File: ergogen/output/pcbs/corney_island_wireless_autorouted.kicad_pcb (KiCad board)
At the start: 2 copper layers, 133.8 x 91.7 mm, 68 parts

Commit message: Update assets
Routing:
- net C4: track 201.2 -> 172.0 mm, vias 2 -> 3
- net R0: track 177.9 -> 203.0 mm, vias 11 -> 9
- net R1: track 164.5 -> 185.3 mm, vias 9 -> 8
- net C3: track 208.1 -> 192.2 mm, vias 2 -> 3
- net C5: track 176.6 -> 161.1 mm, vias 4 -> 3
- net C2: track 184.3 -> 172.7 mm, vias 1 -> 2
- net R2: track 176.0 -> 170.6 mm, vias 7 -> 6
- net SDA: track 53.9 -> 50.1 mm, vias 1 -> 2
- net R3: track 133.9 -> 130.5 mm
- net GND: track 105.8 -> 109.1 mm
- net BAT_P: track 60.6 -> 63.7 mm
- net DISP1_5: track 7.38 -> 4.90 mm
- net DISP1_2: track 7.38 -> 4.90 mm
- net DISP1_4: track 7.38 -> 4.90 mm
- net DISP1_1: track 7.38 -> 4.90 mm
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
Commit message: Update assets
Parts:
- removed SW1: , power_switch
- removed SW2: , sw_reset_side
- added MH1: , ceoloide:mounting_hole_npth, F.Cu at (207.8, 100.5)
- added MH2: , ceoloide:mounting_hole_npth, F.Cu at (222.2, 109.0)
- added MH3: , ceoloide:mounting_hole_npth, F.Cu at (109.5, 71.5)
- added MH4: , ceoloide:mounting_hole_npth, F.Cu at (109.5, 90.5)
- added MH5: , ceoloide:mounting_hole_npth, F.Cu at (185.5, 68.0)
- added MH6: , ceoloide:mounting_hole_npth, F.Cu at (152.7, 107.7)
- added MH7: , ceoloide:mounting_hole_npth, F.Cu at (199.2, 115.3)
- added PWR1: power_switch, ceoloide:power_switch_smd_side, F.Cu at (223.0, 99.0)
- added RST1: reset_button_smd_side, ceoloide:reset_button_smd_side, F.Cu at (214.7, 55.2)
- D1, D10, D11, D12, D13, D14, D15, D16, D17, D18, D19, D2, D20, D21, D22, D23, D24, D25, D26, D27, D28, D29, D3, D30, D31, D32, D33, D34, D35, D36, D37, D38, D39, D4, D40, D41, D42, D5, D6, D7, D8, D9: footprint ComboDiode -> ceoloide:diode_tht_sod123
- DISP1: footprint nice!view -> ceoloide:nice_view
- JST1: footprint JST_PH_S2B-PH-K -> ceoloide/battery_connector_jst_ph_2
- MCU1: footprint nice_nano -> ceoloide:nice_nano
- moved JST1 9.80 mm to (211.8, 97.8), turned to 90 degrees
- moved DISP1 0.50 mm to (214.6, 73.2)
- moved D20 0.40 mm to (195.0, 118.3)
- moved D41 0.40 mm to (180.7, 114.4)
- moved D1 0.40 mm to (107.4, 98.7)
- moved D10 0.40 mm to (164.4, 91.5)
- moved D11 0.40 mm to (164.4, 72.5)
- moved D12 0.40 mm to (164.4, 53.5)
- moved D13 0.40 mm to (183.4, 93.9)
- moved D14 0.40 mm to (183.4, 74.9)
- moved D15 0.40 mm to (183.4, 55.9)
- moved D16 0.40 mm to (202.4, 96.3)
- moved D17 0.40 mm to (202.4, 77.3)
- moved D18 0.40 mm to (202.4, 58.3)
- moved D19 0.40 mm to (173.9, 113.5)
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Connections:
- JST1 pad 1: GND -> BAT_P
- JST1 pad 2: BAT_P -> GND
- MCU1 pad 13: MCU1_13 -> MCU1_12
- MCU1 pad 14: MCU1_14 -> MCU1_11
- MCU1 pad 15: MCU1_15 -> MCU1_10
- MCU1 pad 16: MCU1_16 -> MCU1_9
- MCU1 pad 17: MCU1_17 -> MCU1_8
- MCU1 pad 18: MCU1_18 -> MCU1_7
- MCU1 pad 19: MCU1_19 -> MCU1_6
- MCU1 pad 20: MCU1_20 -> MCU1_5
- MCU1 pad 21: MCU1_21 -> MCU1_4
- MCU1 pad 22: MCU1_22 -> MCU1_3
- MCU1 pad 23: MCU1_23 -> MCU1_2
- MCU1 pad 24: MCU1_24 -> MCU1_1
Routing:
- net C3: track 192.2 -> 237.4 mm, vias 3 -> 4
- net RAW: track 21.2 -> 62.4 mm, vias 0 -> 1
- net BAT_P: track 63.7 -> 25.7 mm, vias 2 -> 1
- net R1: track 185.3 -> 157.4 mm, vias 8 -> 7
- net R0: track 203.0 -> 176.5 mm, vias 9 -> 10
- net C0: track 239.8 -> 216.1 mm
- net RST: track 31.4 -> 49.2 mm, vias 1 -> 0
- net C1: track 193.2 -> 204.6 mm, vias 1 -> 2
- net GND: track 109.1 -> 118.9 mm, vias 2 -> 1
- net C5: track 161.1 -> 152.9 mm, vias 3 -> 4
- net CS: track 48.9 -> 56.2 mm, vias 1 -> 0
- net R2: track 170.6 -> 177.6 mm, vias 6 -> 5
- net R3: track 130.5 -> 123.9 mm, vias 3 -> 4
- net C2: track 172.7 -> 177.1 mm
- net ring_top: track 19.5 -> 23.4 mm
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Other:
- outline, holes or cut-outs redrawn
- net class Default removed

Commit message: Update assets
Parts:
- DISP1: footprint ceoloide:nice_view -> ceoloide:display_nice_view
- JST1: footprint ceoloide/battery_connector_jst_ph_2 -> ceoloide:battery_connector_jst_ph_2
- MCU1: footprint ceoloide:nice_nano -> ceoloide:mcu_nice_nano

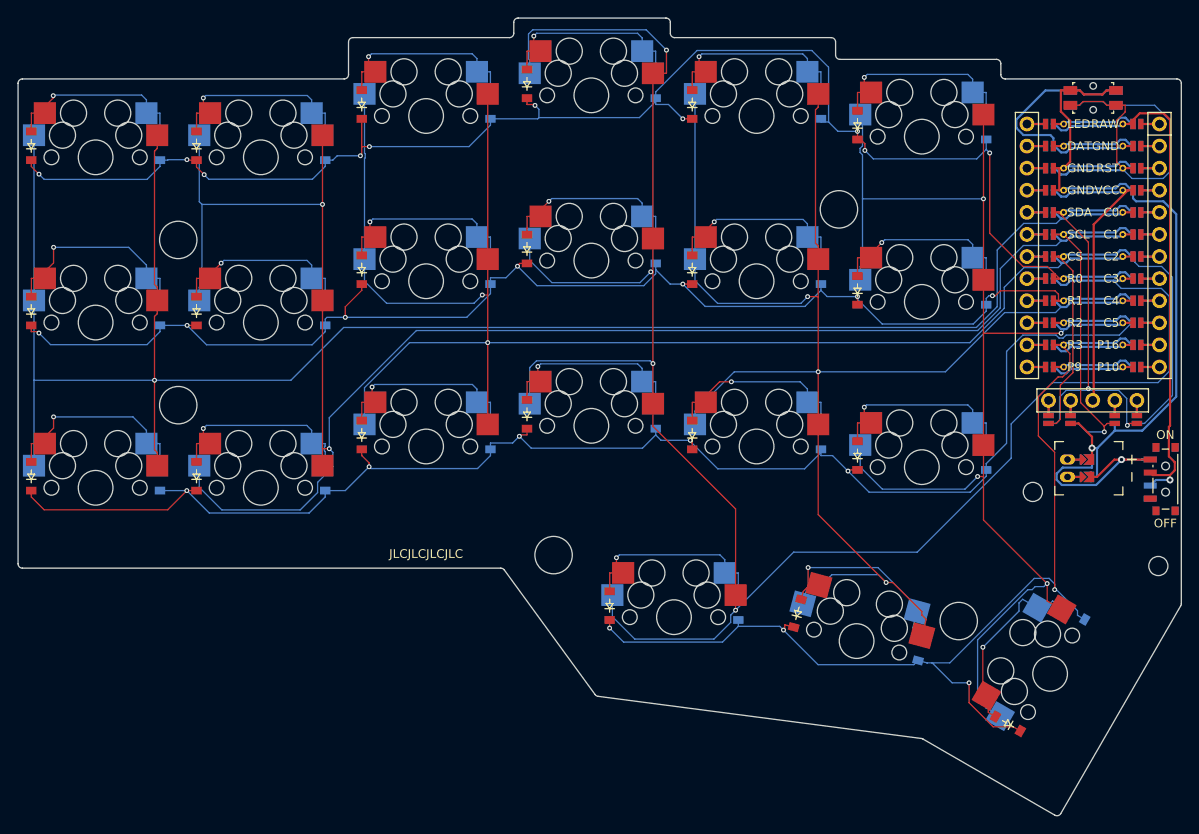
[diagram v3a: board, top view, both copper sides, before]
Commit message: Update footprints library and artifacts
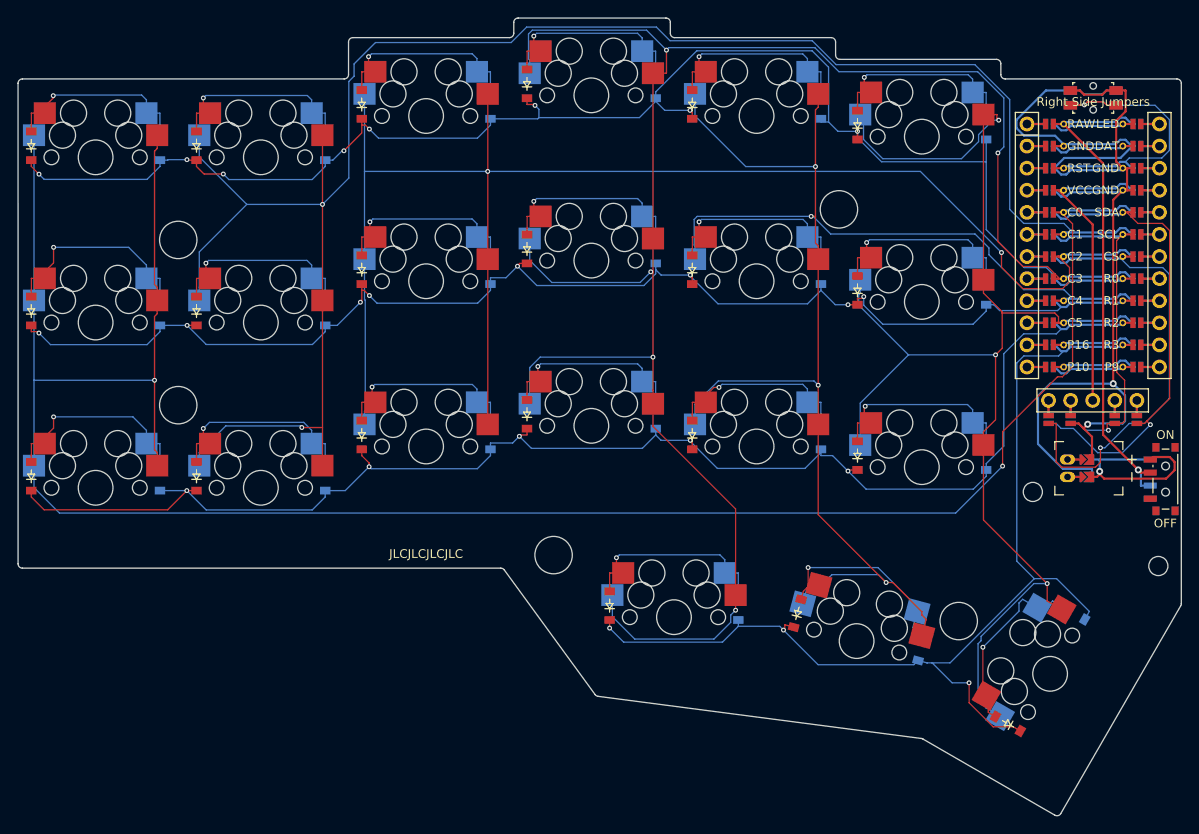
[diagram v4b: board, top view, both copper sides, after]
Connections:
- MCU1 pad 113: P9 -> P10
- MCU1 pad 114: R3 -> P16
- MCU1 pad 115: R2 -> C5
- MCU1 pad 116: R1 -> C4
- MCU1 pad 117: R0 -> C3
- MCU1 pad 118: CS -> C2
- MCU1 pad 119: SCL -> C1
- MCU1 pad 120: SDA -> C0
- MCU1 pad 121: GND -> VCC
- MCU1 pad 122: GND -> RST
- MCU1 pad 123: DAT -> GND
- MCU1 pad 124: LED -> RAW
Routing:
- net C0: track 216.1 -> 251.1 mm, vias 1 -> 2
- net GND: track 118.9 -> 140.9 mm, vias 1 -> 2
- net C3: track 237.4 -> 225.0 mm, vias 4 -> 5
- net RST: track 49.2 -> 37.1 mm, vias 0 -> 1
- net C1: track 204.6 -> 216.5 mm
- net R2: track 177.6 -> 168.4 mm
- net SDA: track 48.7 -> 55.0 mm, vias 2 -> 1
- net C5: track 152.9 -> 158.6 mm, vias 4 -> 3
- net RAW: track 62.4 -> 57.8 mm
- net C4: track 175.8 -> 180.0 mm, vias 3 -> 4
- net R1: track 157.4 -> 154.0 mm, vias 7 -> 8
- net BAT_P: track 25.7 -> 22.7 mm
- net CS: track 56.2 -> 53.4 mm, vias 0 -> 1
- net R0: track 176.5 -> 175.0 mm, vias 10 -> 8
- net pinky_home: track 22.1 -> 23.1 mm
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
